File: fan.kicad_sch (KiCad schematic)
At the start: 16 parts, among them J8 Conn_01x04, J9 Conn_01x04, U7 TMP1075, U8 TMP1075, U9 EMC2302

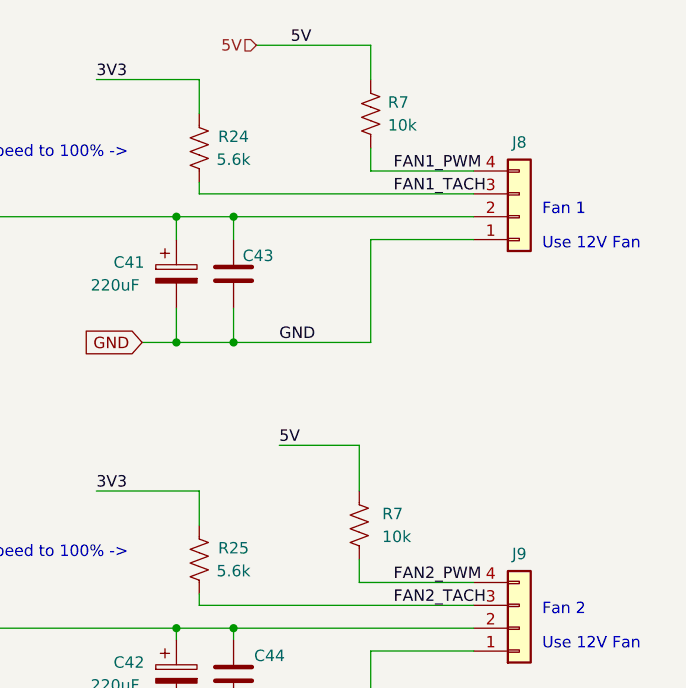
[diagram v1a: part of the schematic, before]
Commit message: updated to KiCad v9, filled in incomplete BOM and exported.
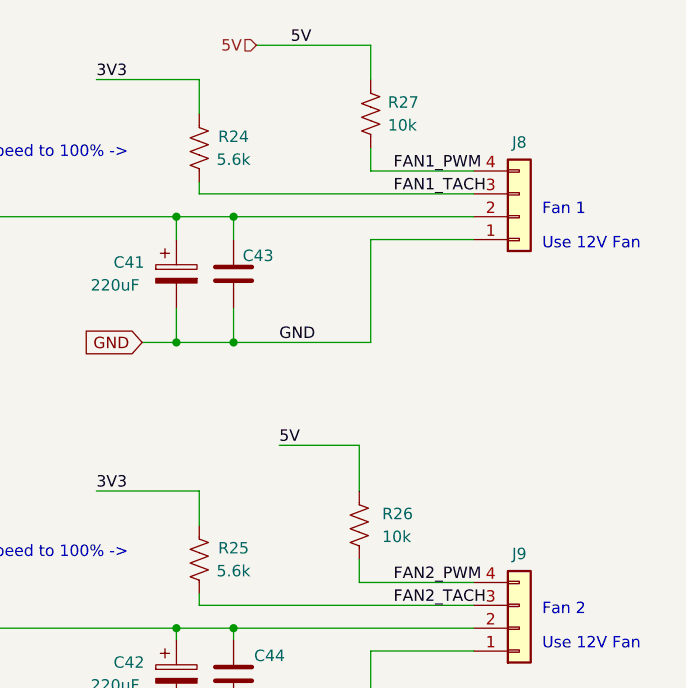
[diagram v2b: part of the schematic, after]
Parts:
- renumbered R7 to R26, R7 to R27
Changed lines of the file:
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@@
 (kicad_sch
-	(version 20231120)
+	(version 20250114)
 	(generator "eeschema")
-	(generator_version "8.0")
+	(generator_version "9.0")
 	(paper "A")
 	(title_block
@@
 		(rev "701")
 	)
+	(text "I2C Address: 0x2E"
+		(exclude_from_sim no)
+		(at 82.55 63.5 0)
+		(effects
+			(font
+				(size 1.27 1.27)
+			)
+			(justify left bottom)
+		)
+	)
+	(text "Temperature Sensors"
+		(exclude_from_sim no)
+		(at 67.31 86.36 0)
+		(effects
+			(font
+				(size 2.5 2.5)
+			)
+			(justify left bottom)
+		)
+	)
+	(text "I2C Address: 0x4A"
+		(exclude_from_sim no)
+		(at 78.74 111.76 0)
+		(effects
+			(font
+				(size 1.27 1.27)
+			)
+			(justify left bottom)
+		)
+	)
+	(text "Fan Control"
+		(exclude_from_sim no)
+		(at 80.01 35.56 0)
+		(effects
+			(font
+				(size 2.5 2.5)
+			)
+			(justify left bottom)
+		)
+	)
+	(text "Fan 1"
+		(exclude_from_sim no)
+		(at 246.38 53.34 0)
+		(effects
+			(font
+				(size 1.27 1.27)
+			)
+			(justify left bottom)
+		)
+	)
+	(text "Use 12V Fan"
+		(exclude_from_sim no)
+		(at 246.38 57.15 0)
+		(effects
+			(font
+				(size 1.27 1.27)
+			)
+			(justify left bottom)
+		)
+	)
+	(text "Use 12V Fan"
+		(exclude_from_sim no)
+		(at 246.38 101.6 0)
+		(effects
+			(font
+				(size 1.27 1.27)
+			)
+			(justify left bottom)
+		)
+	)
+	(text "This sets default fan speed to 100% ->"
+		(exclude_from_sim no)
+		(at 166.37 46.99 0)
+		(effects
+			(font
+				(size 1.27 1.27)
+			)
+			(justify left bottom)
+		)
+	)
+	(text "Fan 2"
+		(exclude_from_sim no)
+		(at 246.38 97.79 0)
+		(effects
+			(font
+				(size 1.27 1.27)
+			)
+			(justify left bottom)
+		)
+	)
+	(text "This sets default fan speed to 100% ->"
+		(exclude_from_sim no)
+		(at 166.37 91.44 0)
+		(effects
+			(font
+				(size 1.27 1.27)
+			)
+			(justify left bottom)
+		)
+	)
+	(text "I2C Address: 0x4B"
+		(exclude_from_sim no)
+		(at 78.74 139.7 0)
+		(effects
+			(font
+				(size 1.27 1.27)
+			)
+			(justify left bottom)
+		)
+	)
 	(junction
 		(at 205.74 111.76)
@@
 		)
 	)
-	(text "I2C Address: 0x2E"
-		(exclude_from_sim no)
-		(at 82.55 63.5 0)
-		(effects
-			(font
-				(size 1.27 1.27)
-			)
-			(justify left bottom)
-		)
-	)
-	(text "Temperature Sensors"
-		(exclude_from_sim no)
-		(at 67.31 86.36 0)
-		(effects
-			(font
-				(size 2.5 2.5)
-			)
-			(justify left bottom)
-		)
-	)
-	(text "I2C Address: 0x4A"
-		(exclude_from_sim no)
-		(at 78.74 111.76 0)
-		(effects
-			(font
-				(size 1.27 1.27)
-			)
-			(justify left bottom)
-		)
-	)
-	(text "Fan Control"
-		(exclude_from_sim no)
-		(at 80.01 35.56 0)
-		(effects
-			(font
-				(size 2.5 2.5)
-			)
-			(justify left bottom)
-		)
-	)
-	(text "Fan 1"
-		(exclude_from_sim no)
-		(at 246.38 53.34 0)
-		(effects
-			(font
-				(size 1.27 1.27)
-			)
-			(justify left bottom)
-		)
-	)
-	(text "Use 12V Fan"
-		(exclude_from_sim no)
-		(at 246.38 57.15 0)
-		(effects
-			(font
-				(size 1.27 1.27)
-			)
-			(justify left bottom)
-		)
-	)
-	(text "Use 12V Fan"
-		(exclude_from_sim no)
-		(at 246.38 101.6 0)
-		(effects
-			(font
-				(size 1.27 1.27)
-			)
-			(justify left bottom)
-		)
-	)
-	(text "This sets default fan speed to 100% ->"
-		(exclude_from_sim no)
-		(at 166.37 46.99 0)
-		(effects
-			(font
-				(size 1.27 1.27)
-			)
-			(justify left bottom)
-		)
-	)
-	(text "Fan 2"
-		(exclude_from_sim no)
-		(at 246.38 97.79 0)
-		(effects
-			(font
-				(size 1.27 1.27)
-			)
-			(justify left bottom)
-		)
-	)
-	(text "This sets default fan speed to 100% ->"
-		(exclude_from_sim no)
-		(at 166.37 91.44 0)
-		(effects
-			(font
-				(size 1.27 1.27)
-			)
-			(justify left bottom)
-		)
-	)
-	(text "I2C Address: 0x4B"
-		(exclude_from_sim no)
-		(at 78.74 139.7 0)
-		(effects
-			(font
-				(size 1.27 1.27)
-			)
-			(justify left bottom)
-		)
-	)
 	(label "GND"
 		(at 110.49 110.49 180)
-		(fields_autoplaced yes)
 		(effects
 			(font
@@
 	(label "SCL"
 		(at 72.39 52.07 0)
-		(fields_autoplaced yes)
 		(effects
 			(font
@@
 	(label "GND"
 		(at 72.39 57.15 0)
-		(fields_autoplaced yes)
 		(effects
 			(font
@@
 	(label "FAN1_TACH"
 		(at 116.84 52.07 180)
-		(fields_autoplaced yes)
 		(effects
 			(font
@@
 	(label "3V3"
 		(at 110.49 93.98 180)
-		(fields_autoplaced yes)
 		(effects
 			(font
@@
 	(label "SDA"
 		(at 68.58 129.54 0)
-		(fields_autoplaced yes)
 		(effects
 			(font
@@
 	(label "3V3"
 		(at 196.85 38.1 0)
-		(fields_autoplaced yes)
 		(effects
 			(font
@@
 	(label "SCL"
 		(at 68.58 99.06 0)
-		(fields_autoplaced yes)
 		(effects
 			(font
@@
 	(label "SDA"
 		(at 68.58 102.87 0)
-		(fields_autoplaced yes)
 		(effects
 			(font
@@
 	(label "FAN2_PWM"
 		(at 116.84 49.53 180)
-		(fields_autoplaced yes)
 		(effects
 			(font
@@
 	(label "SCL"
 		(at 68.58 125.73 0)
-		(fields_autoplaced yes)
 		(effects
 			(font
@@
 	(label "GND"
 		(at 217.17 67.31 0)
-		(fields_autoplaced yes)
 		(effects
 			(font
@@
 	(label "5V"
 		(at 218.44 34.29 0)
-		(fields_autoplaced yes)
 		(effects
 			(font
@@
 	(label "FAN1_PWM"
 		(at 229.87 48.26 0)
-		(fields_autoplaced yes)
 		(effects
 			(font
@@
 	(label "FAN1_PWM"
 		(at 116.84 46.99 180)
-		(fields_autoplaced yes)
 		(effects
 			(font
@@
 	(label "FAN2_TACH"
 		(at 229.87 96.52 0)
-		(fields_autoplaced yes)
 		(effects
 			(font
@@
 	(label "SDA"
 		(at 72.39 49.53 0)
-		(fields_autoplaced yes)
 		(effects
 			(font
@@
 	(label "FAN2_TACH"
 		(at 116.84 54.61 180)
-		(fields_autoplaced yes)
 		(effects
 			(font
@@
 	(label "GND"
 		(at 110.49 138.43 180)
-		(fields_autoplaced yes)
 		(effects
 			(font
@@
 	(label "3V3"
 		(at 196.85 83.82 0)
-		(fields_autoplaced yes)
 		(effects
 			(font
@@
 	(label "3V3"
 		(at 110.49 120.65 180)
-		(fields_autoplaced yes)
 		(effects
 			(font
@@
 	(label "GND"
 		(at 217.17 111.76 0)
-		(fields_autoplaced yes)
 		(effects
 			(font
@@
 	(label "3V3"
 		(at 72.39 46.99 0)
-		(fields_autoplaced yes)
 		(effects
 			(font
@@
 	(label "FAN2_PWM"
 		(at 229.87 93.98 0)
-		(fields_autoplaced yes)
 		(effects
 			(font
@@
 	(label "VIN"
 		(at 152.4 53.34 0)
-		(fields_autoplaced yes)
 		(effects
 			(font
@@
 	(label "5V"
 		(at 217.17 78.74 0)
-		(fields_autoplaced yes)
 		(effects
 			(font
@@
 	(label "FAN1_TACH"
 		(at 229.87 50.8 0)
-		(fields_autoplaced yes)
 		(effects
 			(font
@@
 		(shape input)
 		(at 214.63 34.29 180)
-		(fields_autoplaced yes)
 		(effects
 			(font
@@
 		(shape input)
 		(at 147.32 53.34 180)
-		(fields_autoplaced yes)
 		(effects
 			(font
@@
 		(shape input)
 		(at 72.39 52.07 180)
-		(fields_autoplaced yes)
 		(effects
 			(font
@@
 		(shape input)
 		(at 72.39 49.53 180)
-		(fields_autoplaced yes)
 		(effects
 			(font
@@
 		(shape input)
 		(at 54.61 46.99 180)
-		(fields_autoplaced yes)
 		(effects
 			(font
@@
 		(dnp no)
 		(fields_autoplaced yes)
-		(property "Reference" "R7"
+		(property "Reference" "R27"
 			(at 229.235 40.64 0)
 			(effects
@@
 		(dnp no)
 		(fields_autoplaced yes)
-		(property "Reference" "R7"
+		(property "Reference" "R26"
 			(at 228.6 86.36 0)
 			(effects
